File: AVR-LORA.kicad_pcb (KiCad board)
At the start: 2 copper layers, 51.7 x 29.2 mm, 36 parts, among them J1 Batt, J2 Solar, J3 SMA, J4 CONN_01X14, J5 CONN_01X14, U1 MCP1700-3302E_SOT23, U2 RFM95HW, U3 AVR128DB28, Y1 24MHz, Y2 32768Hz

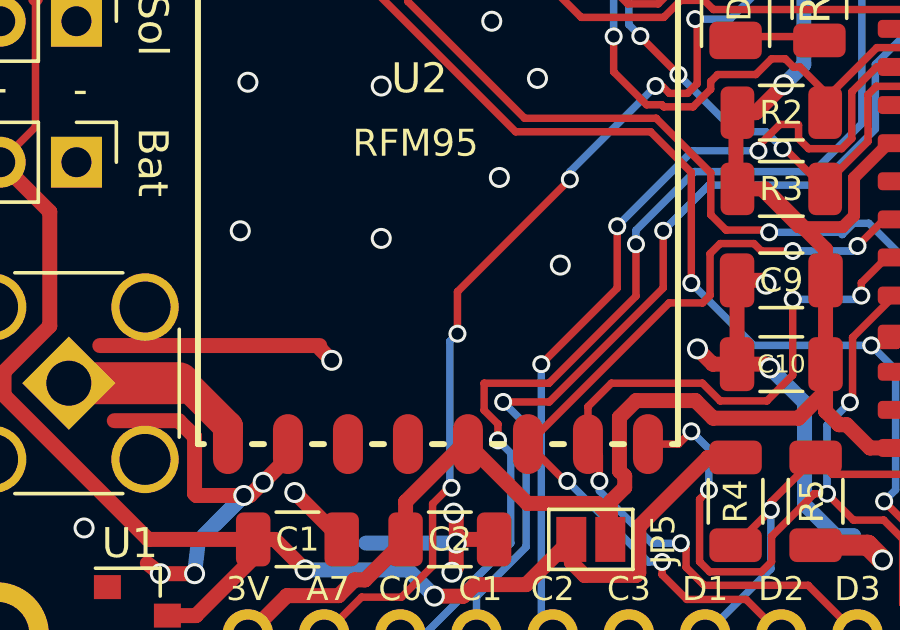
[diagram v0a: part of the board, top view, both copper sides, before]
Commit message: Add KiCAD logo
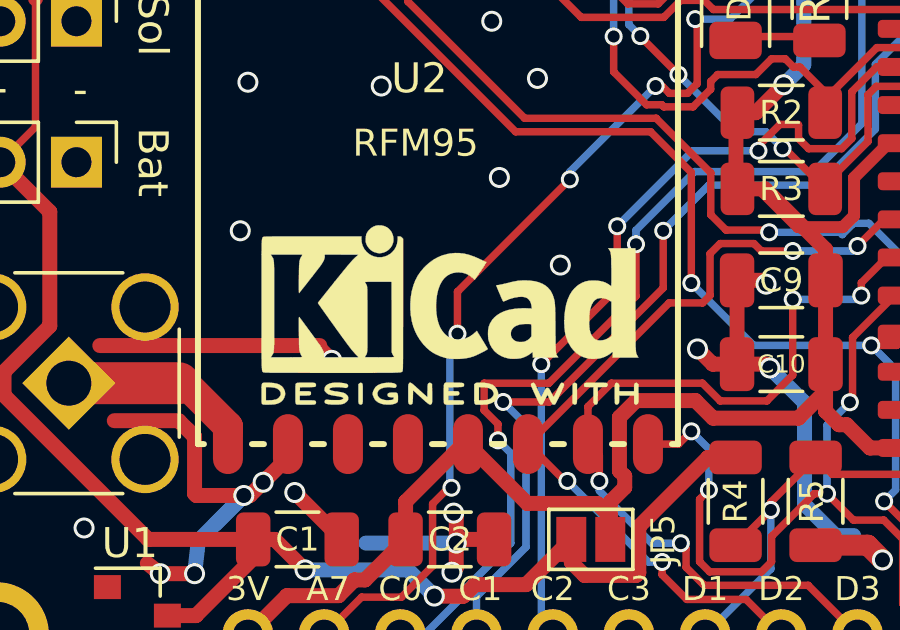
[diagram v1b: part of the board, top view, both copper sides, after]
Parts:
- added REF**: KiCad-Logo2_5mm_SilkScreen, Symbol:KiCad-Logo2_5mm_SilkScreen, F.Cu at (84.7, 98.4)

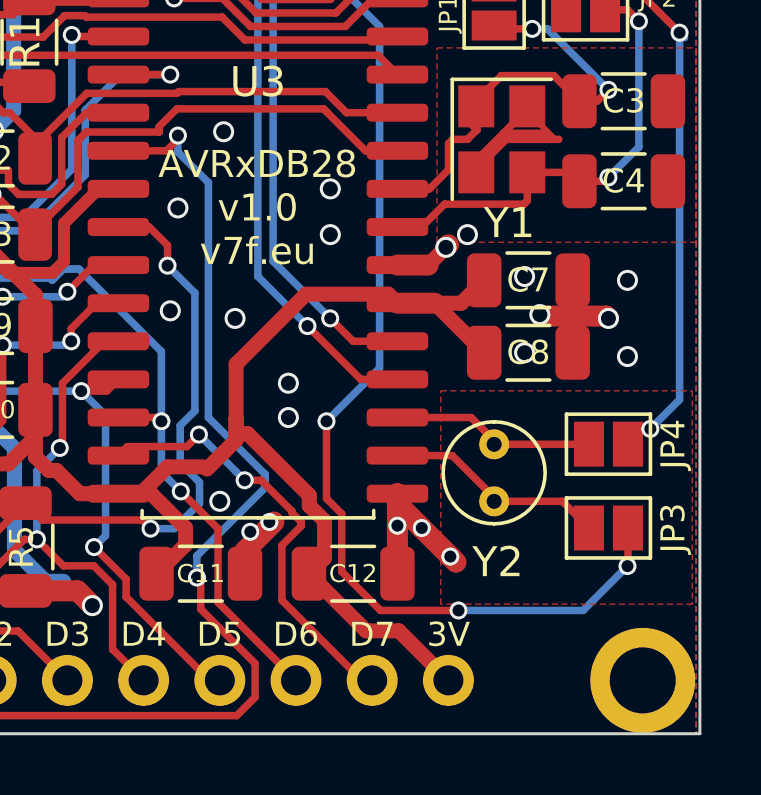
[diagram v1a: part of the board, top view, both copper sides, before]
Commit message: Add capacitors to 32768 crystal for 0805 version
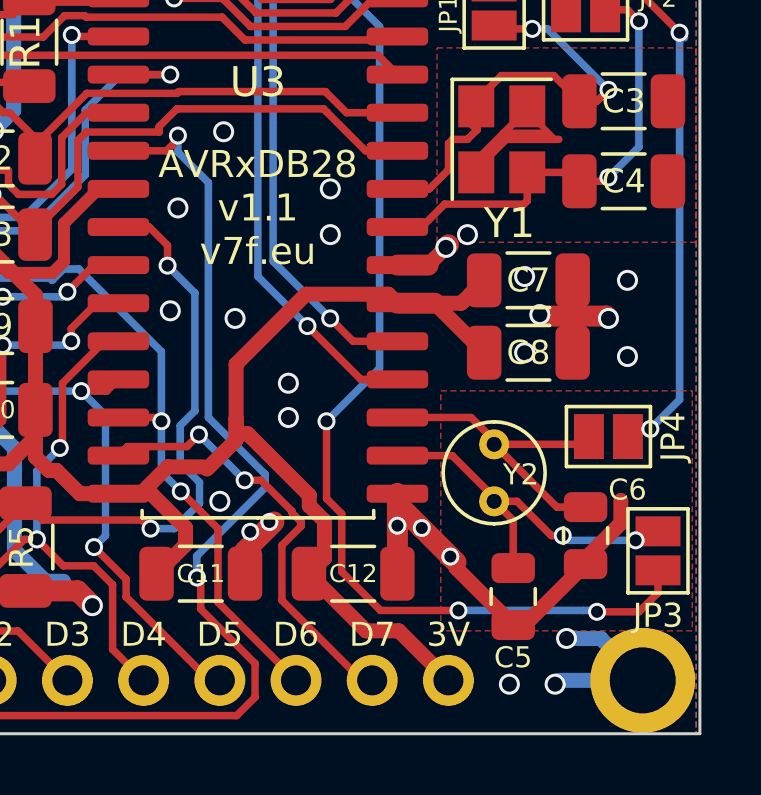
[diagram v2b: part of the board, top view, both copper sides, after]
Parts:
- added C5: 10pF, Capacitor_SMD:C_0805_2012Metric, F.Cu at (113.2, 106.3)
- added C6: 10pF, Capacitor_SMD:C_0805_2012Metric, F.Cu at (115.6, 104.3)
- moved JP3 1.82 mm to (118.0, 104.8), turned to 270 degrees
- moved JP4 0.25 mm to (116.3, 101.0)
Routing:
- net GND: track 81.8 -> 96.7 mm, vias 46 -> 49
- net /F0: track 7.51 -> 13.2 mm, vias 0 -> 2
- net /F1: track 6.88 -> 11.0 mm
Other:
- board text added: "AVRxDB28 v1.1 v7f.eu"
- board text removed: "AVRxDB28 v1.0 v7f.eu"

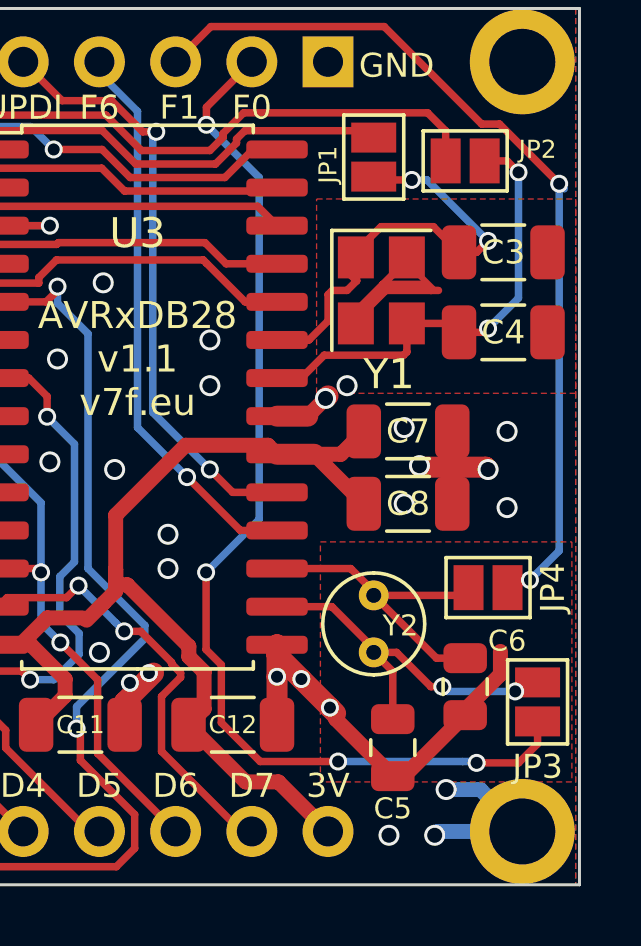
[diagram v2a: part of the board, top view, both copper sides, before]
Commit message: Add capacitors to 32768 crystal for both versions
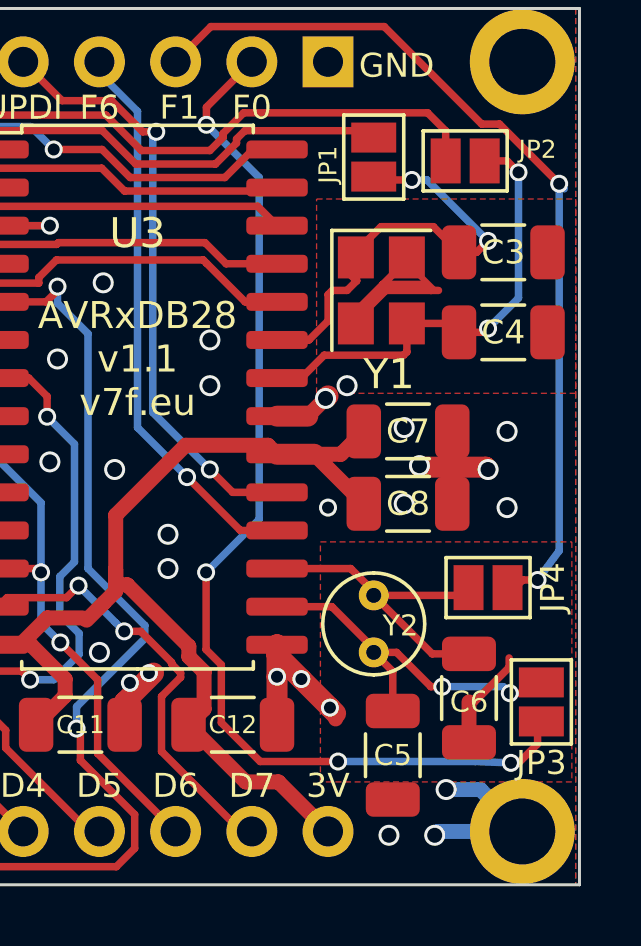
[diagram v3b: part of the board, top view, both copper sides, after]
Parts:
- C5, C6: footprint Capacitor_SMD:C_0805_2012Metric -> Capacitor_SMD:C_1206_3216Metric
- moved C6 0.40 mm to (115.7, 104.6)
- moved C5 0.25 mm to (113.2, 106.6)
- moved JP3 0.13 mm to (118.1, 104.8)
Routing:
- net GND: track 96.7 -> 91.6 mm, vias 49 -> 50
- net /F0: track 13.2 -> 12.6 mm

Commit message: crystal grounding
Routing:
- net GND: vias 50 -> 52

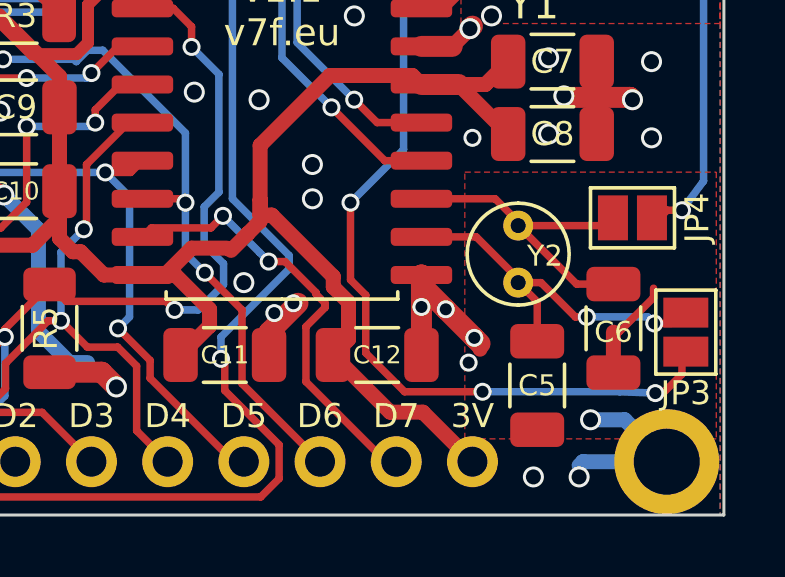
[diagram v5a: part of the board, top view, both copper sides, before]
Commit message: GND tracks
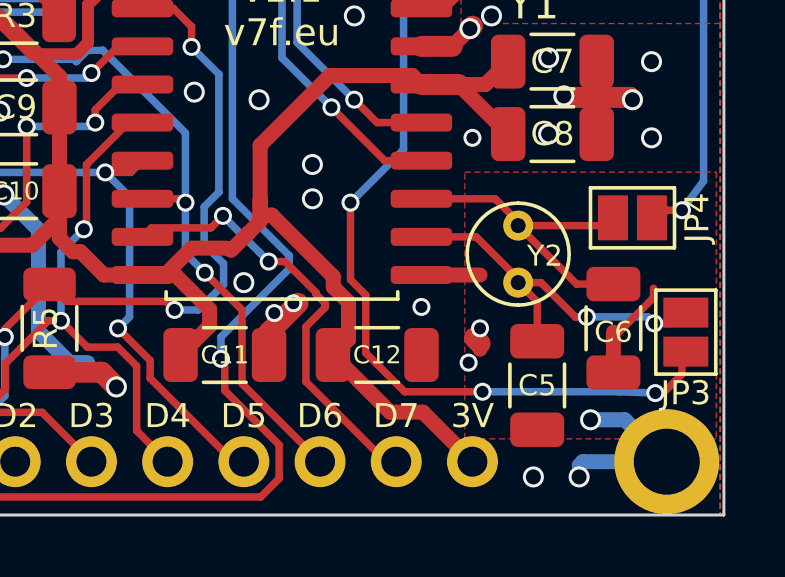
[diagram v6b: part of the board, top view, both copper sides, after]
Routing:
- net GND: track 91.6 -> 88.0 mm, vias 52 -> 51

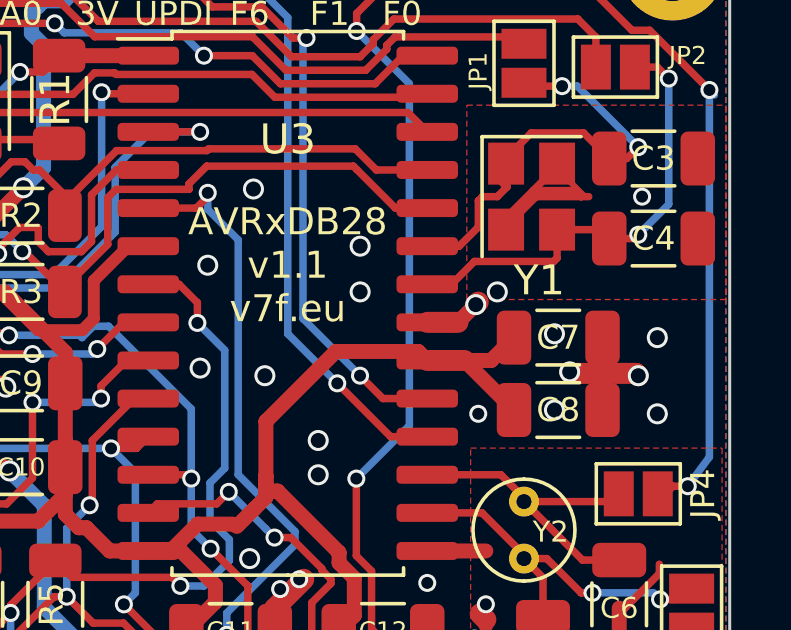
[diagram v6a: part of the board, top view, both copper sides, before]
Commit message: GND tracks
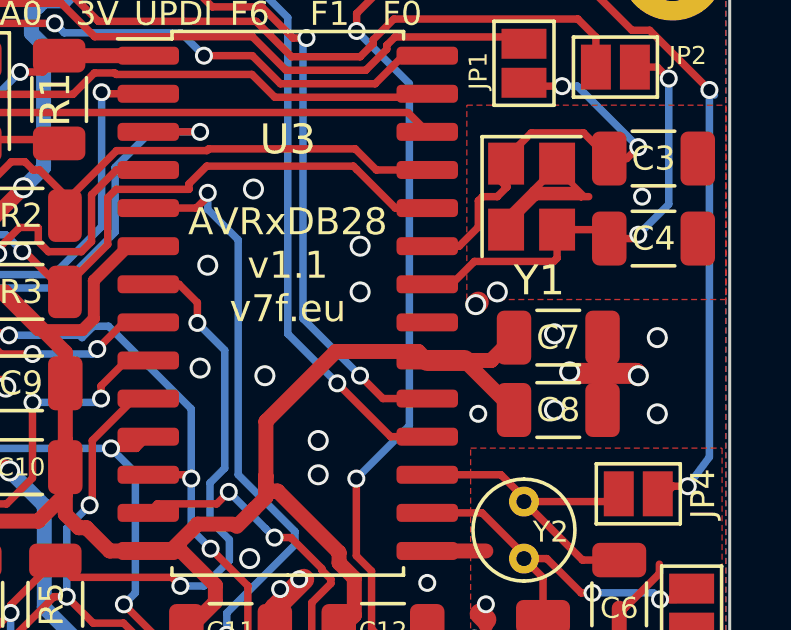
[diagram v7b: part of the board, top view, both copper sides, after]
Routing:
- net GND: track 88.0 -> 86.2 mm

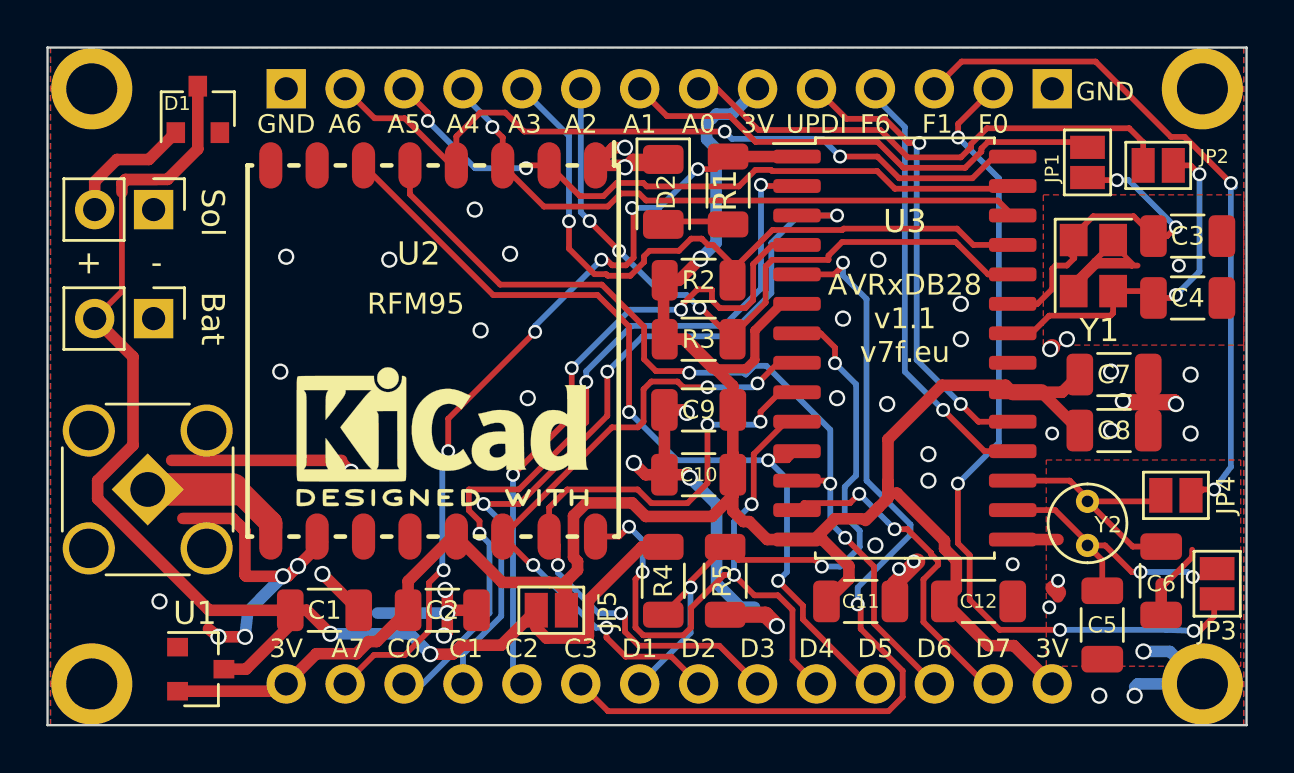
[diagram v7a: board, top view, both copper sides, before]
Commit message: GND VIAs
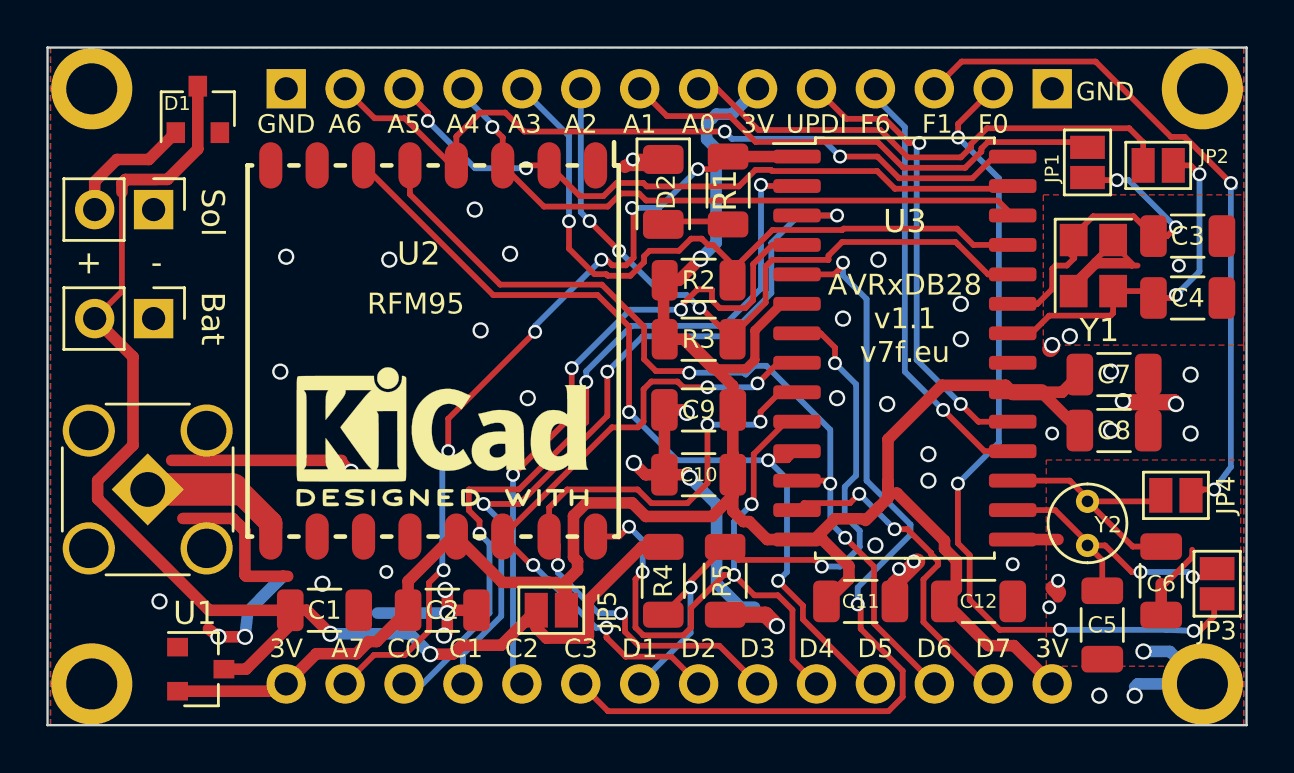
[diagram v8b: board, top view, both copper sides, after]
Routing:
- net GND: track 86.2 -> 77.7 mm, vias 51 -> 49
